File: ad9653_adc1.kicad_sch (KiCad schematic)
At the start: 20 parts, among them J701 142-0701-201, J702 142-0701-201, J703 142-0701-201, J704 142-0701-201, U701 AD9653BCPZ-125

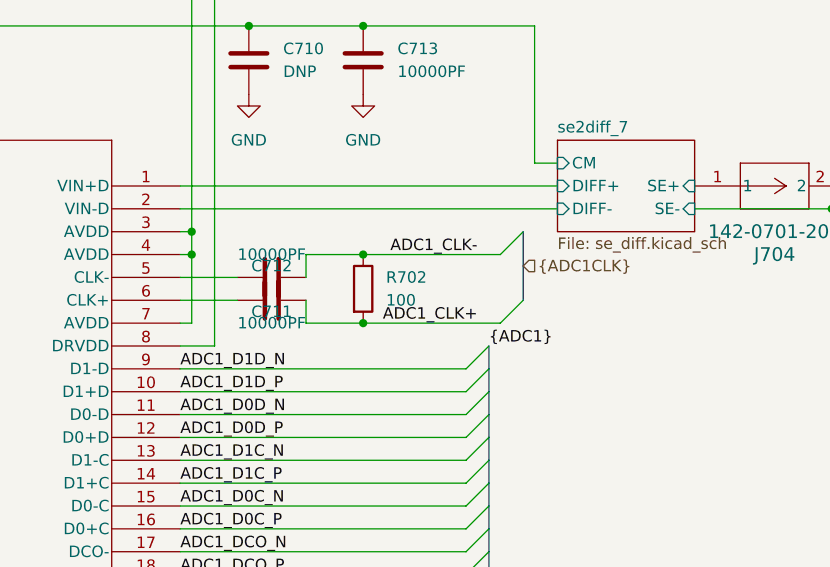
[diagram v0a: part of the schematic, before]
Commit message: fixed differential pair impedance and length matching. Also fixed DRC errors (trace spacing). These are only layout changes, the schematic remains unchanged.
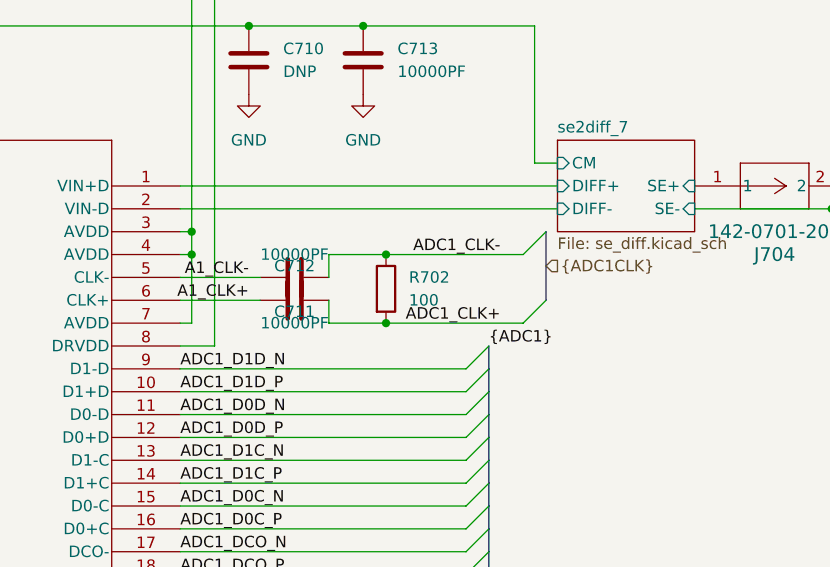
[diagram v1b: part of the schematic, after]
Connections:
- net A1_CLK-: now reaches C711.2, U701.5 (CLK-)
- net A1_CLK+: now reaches C712.2, U701.6 (CLK+)
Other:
- moved on the sheet: C711, C712, R702
